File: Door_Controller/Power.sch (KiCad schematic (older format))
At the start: 7 parts

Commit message: convert grounds to earths
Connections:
- net labels added: Earth
- net labels removed: GNDD
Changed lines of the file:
@@
 Comment4 "Author: Justin Landseadel"
 $EndDescr
-$Comp
-L power:GNDD #PWR?
-U 1 1 5FAFD275
-P 4900 3600
-F 0 "#PWR?" H 4900 3350 50  0001 C CNN
-F 1 "GNDD" H 4904 3445 50  0000 C CNN
-F 2 "" H 4900 3600 50  0001 C CNN
-F 3 "" H 4900 3600 50  0001 C CNN
-	1    4900 3600
-	1    0    0    -1
-$EndComp
 Wire Wire Line
 	4900 3600 4900 3400
@@
 	3250 2600 3150 2600
 $Comp
-L power:GNDD #PWR?
-U 1 1 5FB0AB54
-P 4500 3600
-F 0 "#PWR?" H 4500 3350 50  0001 C CNN
-F 1 "GNDD" H 4504 3445 50  0000 C CNN
-F 2 "" H 4500 3600 50  0001 C CNN
-F 3 "" H 4500 3600 50  0001 C CNN
-	1    4500 3600
-	1    0    0    -1
-$EndComp
-$Comp
 L Device:C C?
 U 1 1 5FB0BB55
@@
 F 3 "~" H 6950 2900 50  0001 C CNN
 	1    6950 2900
-	1    0    0    -1
-$EndComp
-$Comp
-L power:GNDD #PWR?
-U 1 1 5FB0871A
-P 6950 3600
-F 0 "#PWR?" H 6950 3350 50  0001 C CNN
-F 1 "GNDD" H 6954 3445 50  0000 C CNN
-F 2 "" H 6950 3600 50  0001 C CNN
-F 3 "" H 6950 3600 50  0001 C CNN
-	1    6950 3600
 	1    0    0    -1
 $EndComp
@@
 Wire Wire Line
 	3200 4400 4000 4400
+$Comp
+L power:Earth #PWR?
+U 1 1 5FB3EFA0
+P 4500 3600
+F 0 "#PWR?" H 4500 3350 50  0001 C CNN
+F 1 "Earth" H 4500 3450 50  0001 C CNN
+F 2 "" H 4500 3600 50  0001 C CNN
+F 3 "~" H 4500 3600 50  0001 C CNN
+	1    4500 3600
+	1    0    0    -1
+$EndComp
+$Comp
+L power:Earth #PWR?
+U 1 1 5FB3FD3B
+P 4900 3600
+F 0 "#PWR?" H 4900 3350 50  0001 C CNN
+F 1 "Earth" H 4900 3450 50  0001 C CNN
+F 2 "" H 4900 3600 50  0001 C CNN
+F 3 "~" H 4900 3600 50  0001 C CNN
+	1    4900 3600
+	1    0    0    -1
+$EndComp
+$Comp
+L power:Earth #PWR?
+U 1 1 5FB40036
+P 6950 3600
+F 0 "#PWR?" H 6950 3350 50  0001 C CNN
+F 1 "Earth" H 6950 3450 50  0001 C CNN
+F 2 "" H 6950 3600 50  0001 C CNN
+F 3 "~" H 6950 3600 50  0001 C CNN
+	1    6950 3600
+	1    0    0    -1
+$EndComp
 $EndSCHEMATC

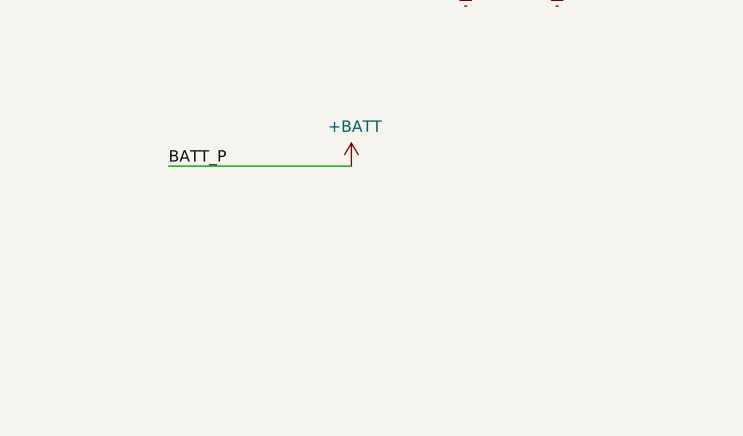
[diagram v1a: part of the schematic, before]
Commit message: add 12V_SNS output to Power Module
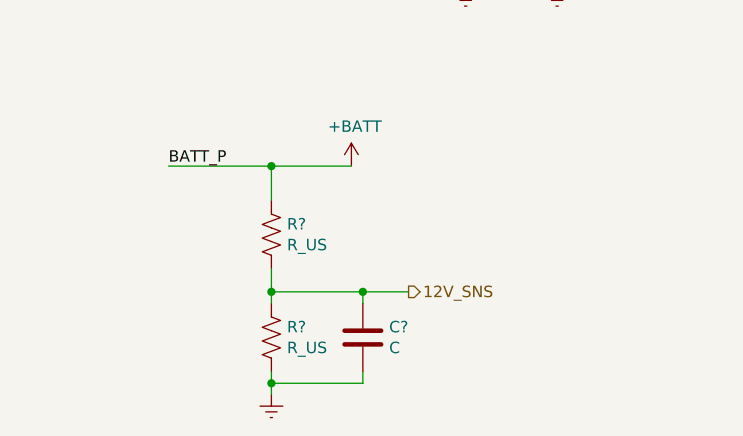
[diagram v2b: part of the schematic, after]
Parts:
- added C?: C, symbol Device:C
- added R? (x2): R_US, symbol Device:R_US
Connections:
- net +BATT: now also R?.1
- net Earth: now also C?.2, R?.2
- new net 12V_SNS: C?.1, R?.1, R?.2
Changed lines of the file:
@@
 $EndComp
 Wire Wire Line
-	3200 4400 4000 4400
+	3200 4400 3650 4400
 $Comp
 L power:Earth #PWR?
@@
 	1    0    0    -1
 $EndComp
+$Comp
+L power:Earth #PWR?
+U 1 1 5FB45EE4
+P 3650 5400
+F 0 "#PWR?" H 3650 5150 50  0001 C CNN
+F 1 "Earth" H 3650 5250 50  0001 C CNN
+F 2 "" H 3650 5400 50  0001 C CNN
+F 3 "~" H 3650 5400 50  0001 C CNN
+	1    3650 5400
+	1    0    0    -1
+$EndComp
+$Comp
+L Device:R_US R?
+U 1 1 5FB46934
+P 3650 4700
+F 0 "R?" H 3718 4746 50  0000 L CNN
+F 1 "R_US" H 3718 4655 50  0000 L CNN
+F 2 "" V 3690 4690 50  0001 C CNN
+F 3 "~" H 3650 4700 50  0001 C CNN
+	1    3650 4700
+	1    0    0    -1
+$EndComp
+$Comp
+L Device:R_US R?
+U 1 1 5FB47867
+P 3650 5150
+F 0 "R?" H 3718 5196 50  0000 L CNN
+F 1 "R_US" H 3718 5105 50  0000 L CNN
+F 2 "" V 3690 5140 50  0001 C CNN
+F 3 "~" H 3650 5150 50  0001 C CNN
+	1    3650 5150
+	1    0    0    -1
+$EndComp
+Text HLabel 4250 4950 2    50   Output ~ 0
+12V_SNS
+Wire Wire Line
+	3650 5400 3650 5350
+Wire Wire Line
+	3650 5000 3650 4950
+Wire Wire Line
+	3650 4550 3650 4400
+Connection ~ 3650 4400
+Wire Wire Line
+	3650 4400 4000 4400
+Wire Wire Line
+	4250 4950 4050 4950
+Connection ~ 3650 4950
+Wire Wire Line
+	3650 4950 3650 4850
+$Comp
+L Device:C C?
+U 1 1 5FB49CED
+P 4050 5150
+F 0 "C?" H 4165 5196 50  0000 L CNN
+F 1 "C" H 4165 5105 50  0000 L CNN
+F 2 "" H 4088 5000 50  0001 C CNN
+F 3 "~" H 4050 5150 50  0001 C CNN
+	1    4050 5150
+	1    0    0    -1
+$EndComp
+Wire Wire Line
+	4050 5000 4050 4950
+Connection ~ 4050 4950
+Wire Wire Line
+	4050 4950 3650 4950
+Wire Wire Line
+	4050 5300 4050 5350
+Wire Wire Line
+	4050 5350 3650 5350
+Connection ~ 3650 5350
+Wire Wire Line
+	3650 5350 3650 5300
 $EndSCHEMATC

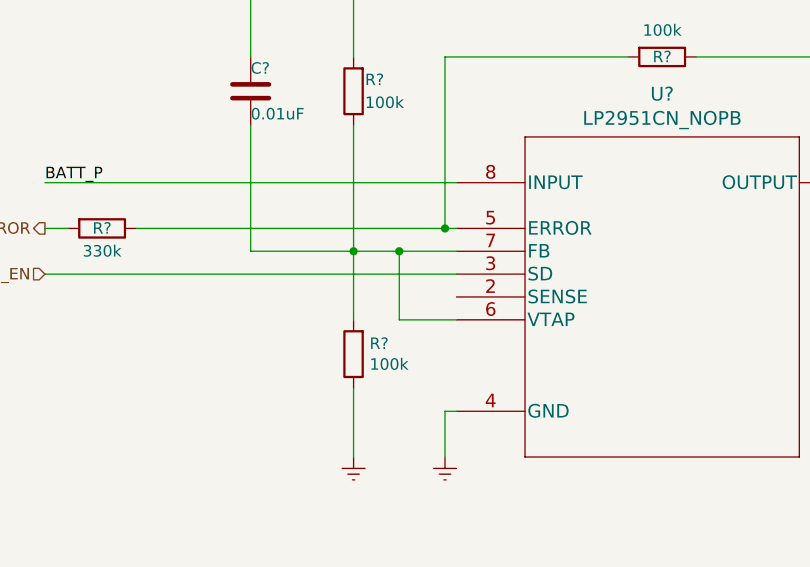
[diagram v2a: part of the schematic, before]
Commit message: rm VTAP-FB connection in Power Module
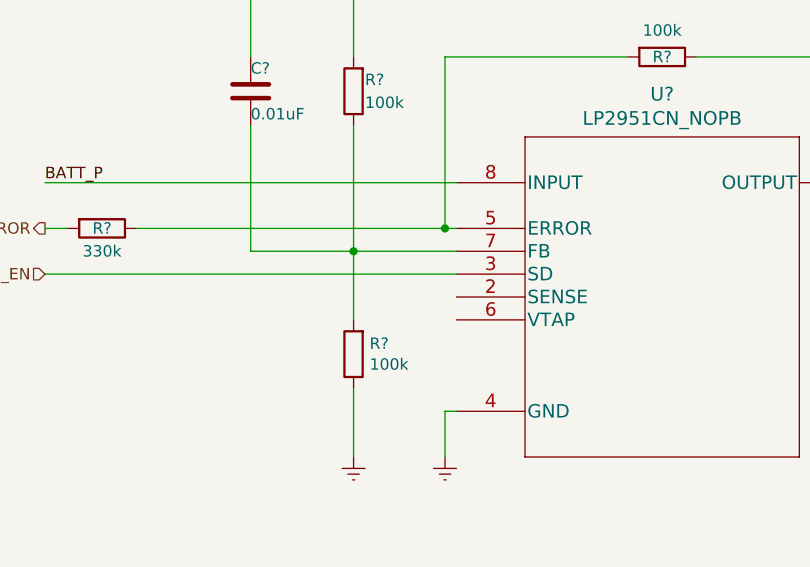
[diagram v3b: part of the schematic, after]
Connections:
- net at C?.2, R?.1, R?.2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: no longer U?.6 (VTAP)
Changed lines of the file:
@@
 	3150 2400 4950 2400
-Wire Wire Line
-	4500 2700 4700 2700
 Wire Wire Line
 	4900 3400 4950 3400
@@
 Wire Wire Line
 	4900 2600 4950 2600
-Wire Wire Line
-	4950 3000 4700 3000
-Wire Wire Line
-	4700 3000 4700 2700
-Connection ~ 4700 2700
-Wire Wire Line
-	4700 2700 4950 2700
 Text Label 3200 4400 0    50   ~ 0
 BATT_P
@@
 Wire Wire Line
 	3650 5350 3650 5300
+Wire Wire Line
+	4500 2700 4950 2700
 $EndSCHEMATC
